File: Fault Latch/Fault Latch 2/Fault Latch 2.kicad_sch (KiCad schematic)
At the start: 105 parts, among them J1 1053141312, J3 1053131202, J4 1053131202, K101 Fujitsu_FTR-LYAA005x, K102 Fujitsu_FTR-LYAA005x, K103 Fujitsu_FTR-LYAA005x, Q101 Q_NPN_BEC, Q102 Q_NPN_BEC, Q103 Q_NPN_BEC, Q104 Q_NPN_BEC, Q105 Q_NMOS_GSD, Q106 Q_NMOS_GSD, Q107 Q_PMOS_GSD, Q108 Q_PMOS_GSD, Q109 Q_PMOS_GSD, Q110 Q_NPN_BEC, Q111 Q_NPN_BEC, Q112 Q_NMOS_GSD, Q113 Q_PMOS_GSD, Q114 Q_NMOS_GSD, Q115 Q_NMOS_GSD, Q116 Q_NMOS_GSD, SW101 SW_Omron_B3FS, SW102 SW_Omron_B3FS, SW103 SW_Omron_B3FS, U101 SFH617A-1, U102 SFH617A-1, U103 SFH617A-1, U104 74AHC1G00, U105 74AHC1G00, U106 74AHC1G00, U107 74LS279, U109 SFH617A-1, U110 SFH617A-1, U117 74AHC1G00, U118 LM555xM, U119 74AHC1G00, U121 SFH617A-1, U2 LM1117DT-5.0

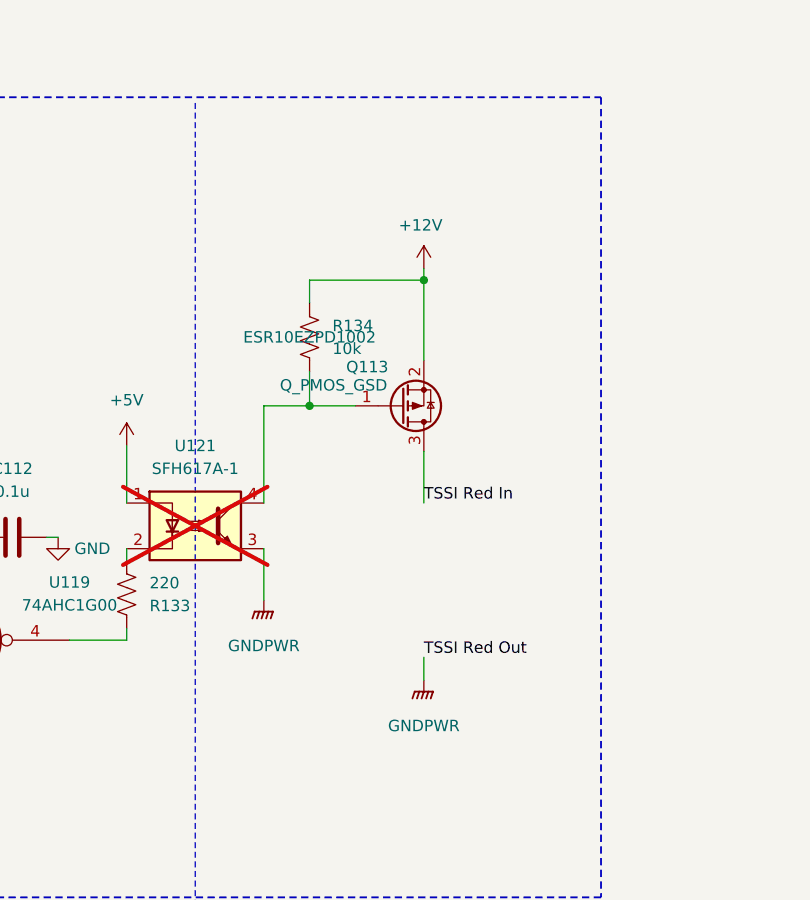
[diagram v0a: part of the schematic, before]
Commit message: Fault Latch pre-BOM check
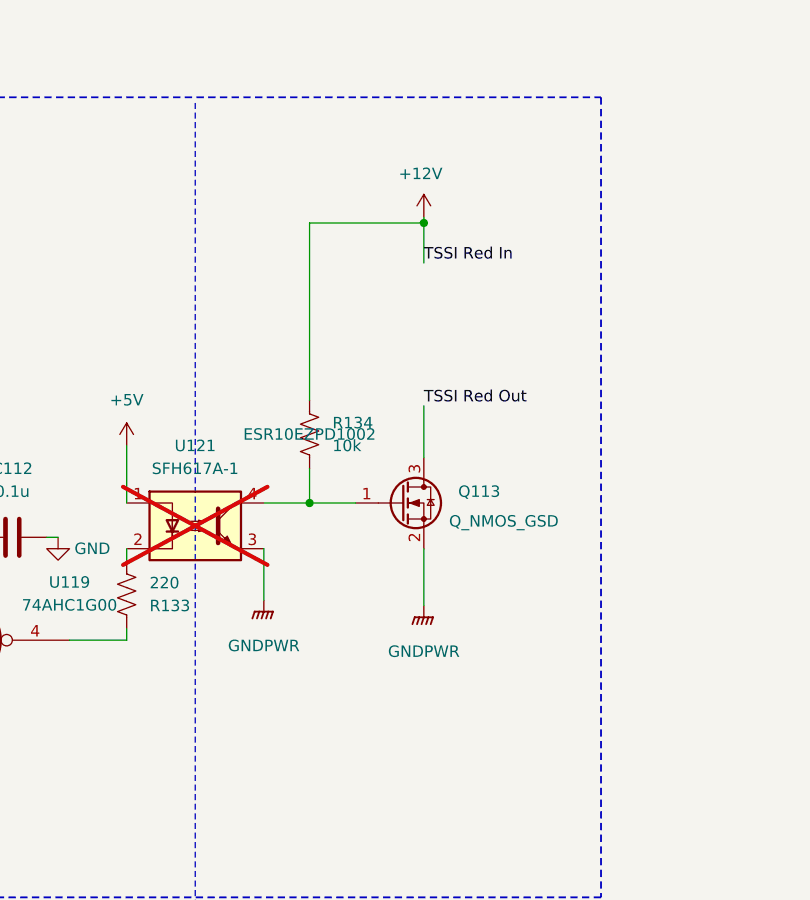
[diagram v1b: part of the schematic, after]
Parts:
- removed Q113: Q_PMOS_GSD, Package_TO_SOT_SMD:SOT-523, symbol Transistor_FET:Q_PMOS_GSD
- added Q113: Q_NMOS_GSD, Package_TO_SOT_SMD:SOT-23, symbol Transistor_FET:Q_NMOS_GSD
- R130: JLC# (none) -> ESR03EZPF2700
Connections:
- net TSSI Red In is gone; now on net +12V: J1.8
- net GND: now also Q113.2 (S); no longer J1.7
- net at R134.2, U121.4: now also Q113.1 (G)
- new net TSSI Red Out: J1.7, Q113.3 (D)
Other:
- moved on the sheet: R134

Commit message: Fault Latch BOM Checked and Safety Circuit
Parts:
- J1: JLC# (none) -> C17318123
- J3, J4: JLC# (none) -> C586242
- K101, K102, K103: JLC# (none) -> C1222376
- U101, U102, U103, U109, U110: JLC# (none) -> C5350
- U107: JLC# (none) -> C41430933
- U121: JLC# (none) -> C5350; MOUSER SFH617A-1X007T -> SFH617A-1

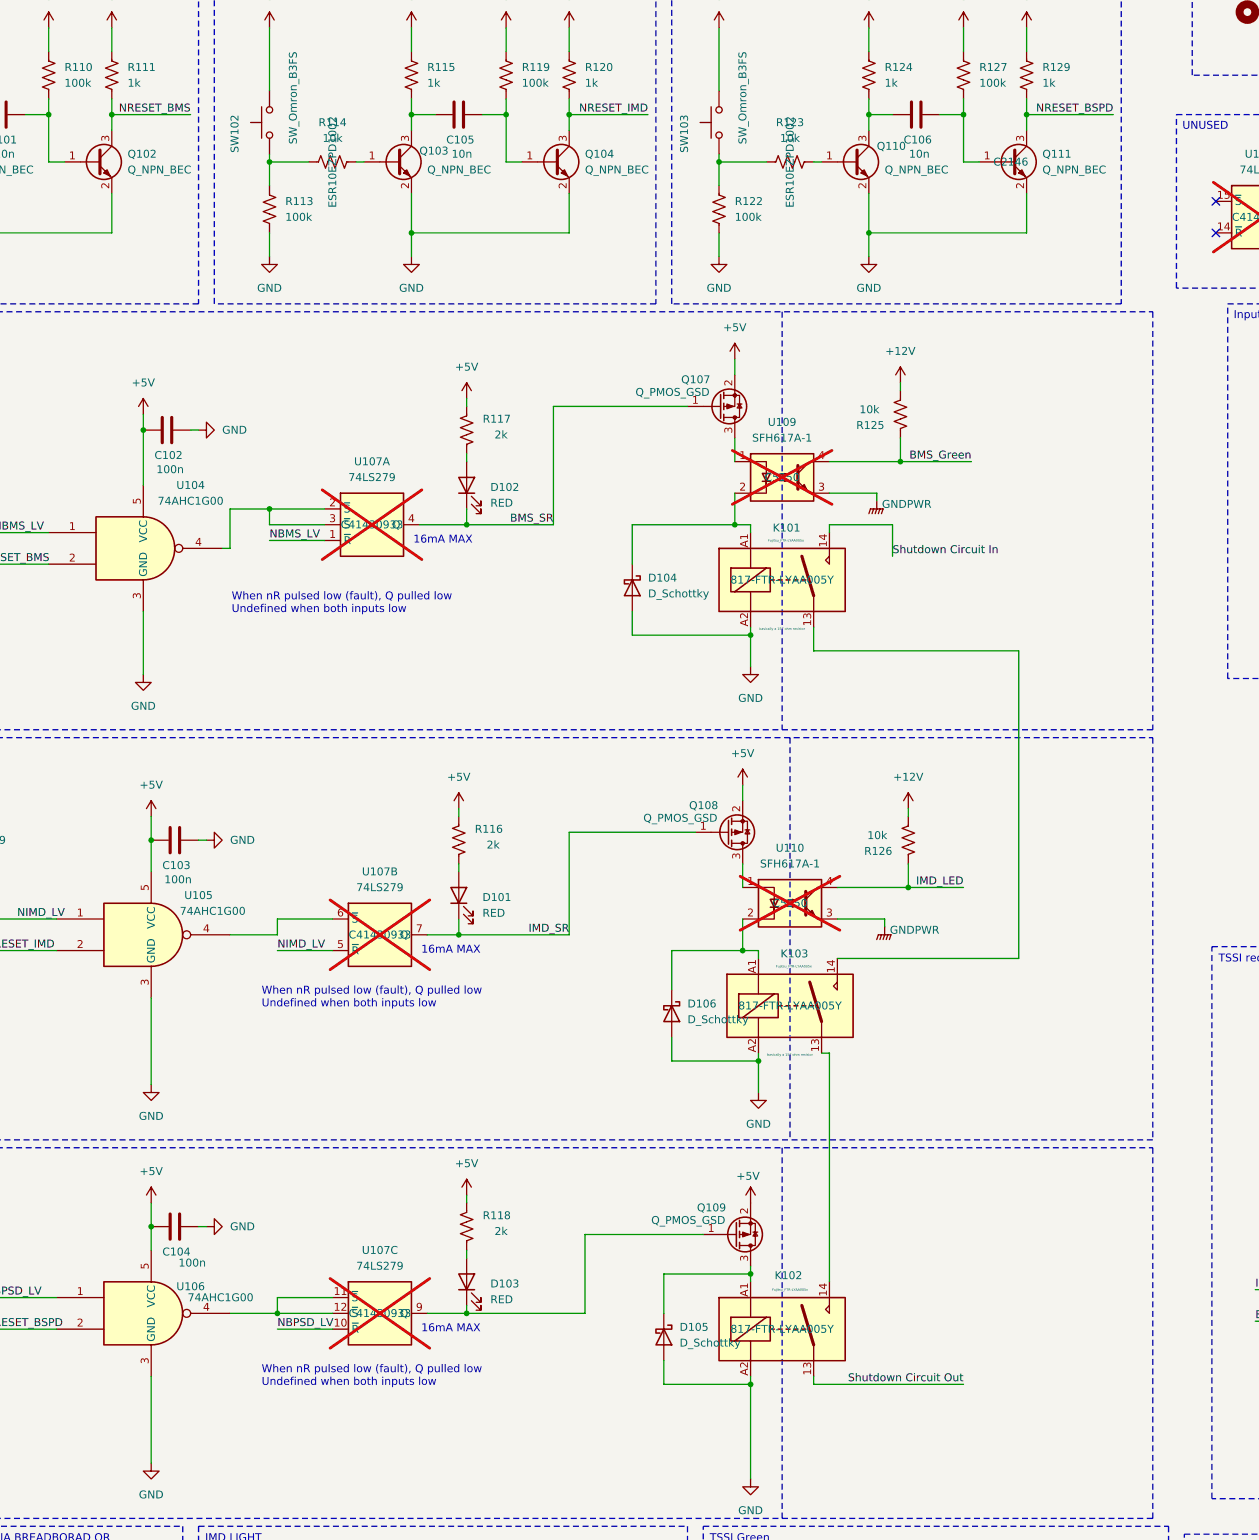
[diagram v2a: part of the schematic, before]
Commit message: Added Measuring points to Fault Latch
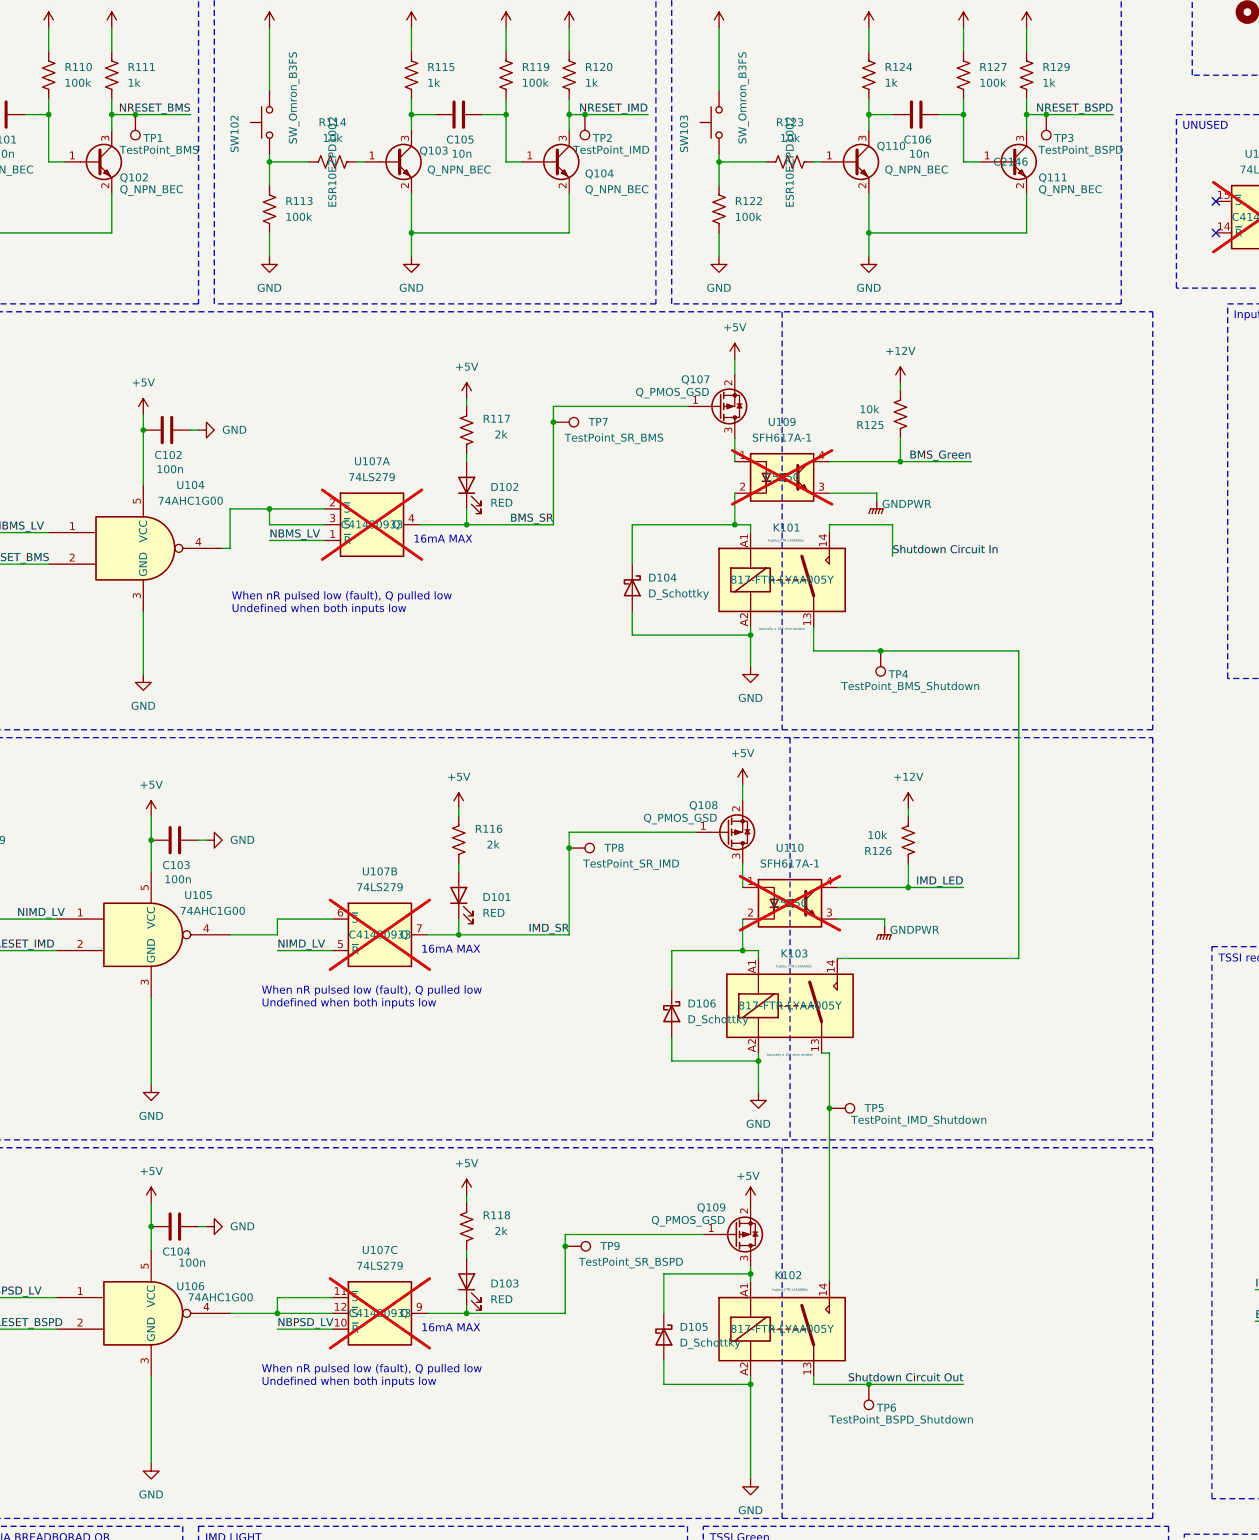
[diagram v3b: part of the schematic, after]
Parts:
- added TP1: TestPoint_BMS, TestPoint:TestPoint_Pad_D1.5mm, symbol Connector:TestPoint
- added TP2: TestPoint_IMD, TestPoint:TestPoint_Pad_D1.5mm, symbol Connector:TestPoint
- added TP3: TestPoint_BSPD, TestPoint:TestPoint_Pad_D1.5mm, symbol Connector:TestPoint
- added TP4: TestPoint_BMS_Shutdown, TestPoint:TestPoint_Pad_D1.5mm, symbol Connector:TestPoint
- added TP5: TestPoint_IMD_Shutdown, TestPoint:TestPoint_Pad_D1.5mm, symbol Connector:TestPoint
- added TP6: TestPoint_BSPD_Shutdown, TestPoint:TestPoint_Pad_D1.5mm, symbol Connector:TestPoint
- added TP7: TestPoint_SR_BMS, TestPoint:TestPoint_Pad_D1.5mm, symbol Connector:TestPoint
- added TP8: TestPoint_SR_IMD, TestPoint:TestPoint_Pad_D1.5mm, symbol Connector:TestPoint
- added TP9: TestPoint_SR_BSPD, TestPoint:TestPoint_Pad_D1.5mm, symbol Connector:TestPoint
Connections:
- net BMS_SR: now also TP7.1
- net IMD_SR: now also TP8.1
- net NRESET_BMS: now also TP1.1
- net NRESET_BSPD: now also TP3.1
- net NRESET_IMD: now also TP2.1
- net Shutdown Circuit Out: now also TP6.1
- net at K102.14, K103.13: now also TP5.1
- net at K101.13, K103.14: now also TP4.1
- net at D103.1 (K), Q109.1 (G), U107.9 (Q): now also TP9.1

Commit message: Fault Latch and RML BOM created
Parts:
- R130: JLC# ESR03EZPF2700 -> C4151887

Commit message: BOM stuff
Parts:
- R102, R103, R104, R133: JLC# C2074007 -> C17557
- R116, R117, R118: JLC# C2889470 -> C1359
- U107: JLC# C41430933 -> C556297
- U118: JLC# C90760 -> (none)

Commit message: Fault Latch Spring Semester
Fixed TSSI, Logic, and everything.
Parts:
- removed C103, C104: 100n, Capacitor_SMD:C_0603_1608Metric_Pad1.08x0.95mm_HandSolder, symbol Device:C
- removed D101, D103: RED, LED_SMD:LED_0805_2012Metric_Pad1.15x1.40mm_HandSolder, symbol Device:LED
- removed D105, D106, D107: D_Schottky, Diode_SMD:D_SMA, symbol Device:D_Schottky
- removed K101, K102, K103: Fujitsu_FTR-LYAA005x, Relay_THT:Relay_SPST-NO_Fujitsu_FTR-LYAA005x_FormA_Vertical, symbol Relay:Fujitsu_FTR-LYAA005x
- removed Q107, Q108, Q109: Q_PMOS_GSD, Package_TO_SOT_SMD:SOT-523, symbol Transistor_FET:Q_PMOS_GSD
- removed Q116: Q_NMOS_GSD, Package_TO_SOT_SMD:SOT-23, symbol Transistor_FET:Q_NMOS_GSD
- removed R103, R104: 220, Resistor_SMD:R_0805_2012Metric_Pad1.20x1.40mm_HandSolder, symbol Device:R_US
- removed R107, R109: 1k, Resistor_SMD:R_0805_2012Metric_Pad1.20x1.40mm_HandSolder, symbol Device:R_US
- removed R116, R118: 2k, Resistor_SMD:R_0805_2012Metric_Pad1.20x1.40mm_HandSolder, symbol Device:R_US
- removed R138: 10k, Resistor_SMD:R_0805_2012Metric_Pad1.20x1.40mm_HandSolder, symbol Device:R_US
- removed TP5: TestPoint_IMD_Shutdown, TestPoint:TestPoint_Pad_D1.5mm, symbol Connector:TestPoint
- removed TP8: TestPoint_SR_IMD, TestPoint:TestPoint_Pad_D1.5mm, symbol Connector:TestPoint
- removed TP9: TestPoint_SR_BSPD, TestPoint:TestPoint_Pad_D1.5mm, symbol Connector:TestPoint
- removed U102, U103, U109, U110, U121: SFH617A-1, Package_DIP:DIP-4_W7.62mm, symbol Isolator:SFH617A-1
- removed U105, U106, U119: 74AHC1G00, Package_TO_SOT_SMD:SOT-23-5, symbol 74xGxx:74AHC1G00
- removed U107: 74LS279, Package_SO:SOIC-16_3.9x9.9mm_P1.27mm, symbol 74xx:74LS279
- added C118: 0.1u, Capacitor_SMD:C_0402_1005Metric, symbol Device:C
- added C119, C120: 100n, Capacitor_SMD:C_0603_1608Metric_Pad1.08x0.95mm_HandSolder, symbol Device:C
- added D107, D109: RED, LED_SMD:LED_0805_2012Metric_Pad1.15x1.40mm_HandSolder, symbol Device:LED
- added D110: D_Schottky, Diode_SMD:D_SMA, symbol Device:D_Schottky
- added K3, K5, K6: Fujitsu_FTR-LYCA005x, Relay_THT:Relay_SPDT_Fujitsu_FTR-LYCA005x_FormC_Vertical, symbol Relay:Fujitsu_FTR-LYCA005x
- added Q117, Q118, Q120: Q_NMOS_GSD, Package_TO_SOT_SMD:SOT-23, symbol Transistor_FET:Q_NMOS_GSD
- added R128: 2k, Resistor_SMD:R_0805_2012Metric_Pad1.20x1.40mm_HandSolder, symbol Device:R_US
- added TP10, TP12: TestPoint_SR_BMS, TestPoint:TestPoint_Pad_D1.5mm, symbol Connector:TestPoint
- added TP11: TestPoint_IMD_Shutdown, TestPoint:TestPoint_Pad_D1.5mm, symbol Connector:TestPoint
- added U1: 74LS279, Package_SO:SOIC-16_3.9x9.9mm_P1.27mm, symbol 74xx:74LS279
- added U108, U111: SFH617A-1, Package_DIP:DIP-4_W7.62mm, symbol Isolator:SFH617A-1
- added U109, U112: 74AHC1G00, Package_TO_SOT_SMD:SOT-23-5, symbol 74xGxx:74AHC1G00
- added U7, U8: SN74AHC1G08DBVR, Package_TO_SOT_SMD:SOT-23-5, symbol 74xGxx:74AHC1G08
- R125: value 10k -> 220; JLC# C17414 -> C17557; MOUSER ESR10EZPD1002 -> (none)
- R126, R134: value 10k -> 1k; JLC# C17414 -> C2889437; MOUSER ESR10EZPD1002 -> (none)
- R137: value 10k -> 2k; JLC# C17414 -> C1359; MOUSER ESR10EZPD1002 -> (none)
- U118: JLC# (none) -> C90760; Manufacturer_Name (none) -> LMC555CMX/NOPB; Mouser Part Number (none) -> 926-LMC555CMX/NOPB
- U2: MOUSER (none) -> 926-LMC555CMX/NOPB
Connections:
- net +12V: now also R125.2, R133.2; no longer R125.1, R126.1, R134.1, R137.1
- net +5V: now also D104.1 (K), D108.1 (K), R126.1, R134.1, R137.2, C118.2, C119.1, C120.1, D110.1 (K), K3.A1, K5.A1, K6.A1, R128.2, U1.16 (VCC), U109.5 (VCC), U112.5 (VCC), U7.5 (VCC), U8.5 (VCC)
- net BMS_SR: now also Q114.1 (G), Q117.1 (G), U1.4 (Q), U8.1
- net BSPD_HV: now also U111.2
- net CLOCK: now also U7.2
- net GND: now also C118.1, C119.2, C120.2, K3.12, K5.12, Q117.2 (S), Q118.2 (S), Q120.2 (S), U1.8 (GND), U108.3, U109.3 (GND), U111.3, U112.3 (GND), U7.3 (GND), U8.3 (GND); no longer D104.2 (A)
- net IMD_HV: now also U108.2
- net IMD_SR: now also Q105.1 (G), D107.1 (K), Q118.1 (G), TP10.1, U1.7 (Q), U8.2
- net NBMS_LV: now also U1.1 (~{R})
- net NBPSD_LV: now also R134.2, U1.10 (~{R}), U111.4, U112.1
- net NIMD_LV: now also R126.2, U1.5 (~{R}), U108.4, U109.1
- net NRESET_BSPD: now also U112.2
- net NRESET_IMD: now also U109.2
- net Shutdown Circuit In: now also K3.14
- net Shutdown Circuit Out: now also K6.11
- net at D108.2 (A): now also K5.A2, Q118.3 (D); no longer R137.2
- net at Q112.1 (G): now also U8.4
- net at TP4.1: now also K3.11, K5.14
- net at R133.1: now also U111.1
- net at Q113.1 (G): now also U7.4; no longer R134.2
- net at U117.4: now also U7.1
- net at U104.4: now also U1.2 (~{S}), U1.3 (~{S})
- removed net BMS_Green: D108.1 (K), Q114.1 (G), R125.2
- removed net IMD_LED: Q105.1 (G), R126.2
- new net: D104.2 (A), K3.A2, Q117.3 (D)
- new net: D109.1 (K), Q120.1 (G), TP12.1, U1.9 (Q)
- new net: D109.2 (A), R137.1
- new net: D107.2 (A), R128.1
- new net: U1.6 (~{S}), U109.4
- new net: K5.11, K6.14, TP11.1
- new net: U1.11 (~{S}), U1.12 (~{S}), U112.4
- new net: R125.1, U108.1
- new net: D110.2 (A), K6.A2, Q120.3 (D)
- no-connect marks 5 -> 6
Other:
- moved on the sheet: C102, C107, C108, C109, C110, C111, C112, D102, D104, J1, J3, J4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
